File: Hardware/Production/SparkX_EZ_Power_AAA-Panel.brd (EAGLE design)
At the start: 187.2 x 136.7 mm, 1236 parts, among them J10 AVR_SPI_PROG_3X2TESTPOINTS, J12 AVR_SPI_PROG_3X2TESTPOINTS, J14 AVR_SPI_PROG_3X2TESTPOINTS, J16 AVR_SPI_PROG_3X2TESTPOINTS, J18 AVR_SPI_PROG_3X2TESTPOINTS, J20 AVR_SPI_PROG_3X2TESTPOINTS, J22 AVR_SPI_PROG_3X2TESTPOINTS, J24 AVR_SPI_PROG_3X2TESTPOINTS, J26 AVR_SPI_PROG_3X2TESTPOINTS, J28 AVR_SPI_PROG_3X2TESTPOINTS, J3 AVR_SPI_PROG_3X2TESTPOINTS, J30 AVR_SPI_PROG_3X2TESTPOINTS, J32 AVR_SPI_PROG_3X2TESTPOINTS, J34 AVR_SPI_PROG_3X2TESTPOINTS, J36 AVR_SPI_PROG_3X2TESTPOINTS, J38 AVR_SPI_PROG_3X2TESTPOINTS, J4 AVR_SPI_PROG_3X2TESTPOINTS, J40 AVR_SPI_PROG_3X2TESTPOINTS, J42 AVR_SPI_PROG_3X2TESTPOINTS, J44 AVR_SPI_PROG_3X2TESTPOINTS, J46 AVR_SPI_PROG_3X2TESTPOINTS, J48 AVR_SPI_PROG_3X2TESTPOINTS, J50 AVR_SPI_PROG_3X2TESTPOINTS, J52 AVR_SPI_PROG_3X2TESTPOINTS, J54 AVR_SPI_PROG_3X2TESTPOINTS, J56 AVR_SPI_PROG_3X2TESTPOINTS, J58 AVR_SPI_PROG_3X2TESTPOINTS, J6 AVR_SPI_PROG_3X2TESTPOINTS, J60 AVR_SPI_PROG_3X2TESTPOINTS, J8 AVR_SPI_PROG_3X2TESTPOINTS, U1 ATTINY43_QFN20, U10 TPS61200, U11 ATTINY43_QFN20, U12 TPS61200, U13 ATTINY43_QFN20, U14 TPS61200, U15 ATTINY43_QFN20, U16 TPS61200, U17 ATTINY43_QFN20, U18 TPS61200, U19 ATTINY43_QFN20, U2 TPS61200, U20 TPS61200, U21 ATTINY43_QFN20, U22 TPS61200, U23 ATTINY43_QFN20, U24 TPS61200, U25 ATTINY43_QFN20, U26 TPS61200, U27 ATTINY43_QFN20, U28 TPS61200, U29 ATTINY43_QFN20, U3 ATTINY43_QFN20, U30 TPS61200, U31 ATTINY43_QFN20, U32 TPS61200, U33 ATTINY43_QFN20, U34 TPS61200, U35 ATTINY43_QFN20, U36 TPS61200, U37 ATTINY43_QFN20, U38 TPS61200, U39 ATTINY43_QFN20, U4 TPS61200, U40 TPS61200, U41 ATTINY43_QFN20, U42 TPS61200, U43 ATTINY43_QFN20, U44 TPS61200, U45 ATTINY43_QFN20, U46 TPS61200, U47 ATTINY43_QFN20, U48 TPS61200, U49 ATTINY43_QFN20, U5 ATTINY43_QFN20, U50 TPS61200, U51 ATTINY43_QFN20, U52 TPS61200, U53 ATTINY43_QFN20, U54 TPS61200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

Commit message: Post-review updates
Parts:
- added RXD, RXD1, RXD10, RXD11, RXD12, RXD13, RXD14, RXD15, RXD16, RXD17, RXD18, RXD19, RXD2, RXD20, RXD21, RXD22, RXD23, RXD24, RXD25, RXD26, RXD27, RXD28, RXD29, RXD3, RXD4, RXD5, RXD6, RXD7, RXD8, RXD9, TXD, TXD1, TXD10, TXD11, TXD12, TXD13, TXD14, TXD15, TXD16, TXD17, TXD18, TXD19, TXD2, TXD20, TXD21, TXD22, TXD23, TXD24, TXD25, TXD26, TXD27, TXD28, TXD29, TXD3, TXD4, TXD5, TXD6, TXD7, TXD8, TXD9: TEST-POINT3X4, SparkFun-Connectors:PAD.03X.04
- added U$301, U$303, U$313, U$315, U$325, U$327, U$337, U$339, U$349, U$351: SPARKX-LOGO3, SparkX:SPARKX-SMALL
- added U$302, U$314, U$326, U$338, U$350: (no value), output:#OUT#0
- added U$304, U$316, U$328, U$340, U$352: (no value), output:#IN#0
- added U$305, U$317, U$329, U$341, U$353: (no value), output:#VIN#0
- added U$306, U$318, U$330, U$342, U$354: (no value), output:#3V3_EN#0
- added U$307, U$319, U$331, U$343, U$355: (no value), output:#PROC_PWR#0
- added U$308, U$320, U$332, U$344, U$356: (no value), output:#AT_VCC#0
- added U$309, U$310, U$321, U$322, U$333, U$334, U$345, U$346, U$357, U$358: (no value), output:EZ_POWER_AAA0
- added U$311, U$323, U$335, U$347, U$359: (no value), output:#TXD#0
- added U$312, U$324, U$336, U$348, U$360: (no value), output:#RXD#0
- C1, C103, C111, C119, C127, C135, C143, C15, C151, C159, C167, C175, C183, C191, C199, C207, C215, C223, C23, C231, C239, C31, C39, C47, C55, C63, C71, C79, C87, C95: device SparkFun-Capacitors:0603 -> SparkFun-Capacitors:0402-TIGHT
- C101, C102, C104, C109, C110, C112, C117, C118, C120, C125, C126, C128, C13, C133, C134, C136, C14, C141, C142, C144, C149, C150, C152, C157, C158, C16, C160, C165, C166, C168, C173, C174, C176, C181, C182, C184, C189, C190, C192, C197, C198, C2, C200, C205, C206, C208, C21, C213, C214, C216, C22, C221, C222, C224, C229, C230, C232, C237, C238, C24, C240, C29, C30, C32, C37, C38, C4, C40, C45, C46, C48, C53, C54, C56, C6, C61, C62, C64, C69, C70, C72, C77, C78, C80, C85, C86, C88, C93, C94, C96: device SparkFun-Capacitors:0402 -> SparkFun-Capacitors:0402-TIGHT
- L10, L12, L14, L16, L18, L2, L20, L22, L24, L26, L28, L30, L32, L34, L36, L38, L4, L40, L42, L44, L46, L48, L50, L52, L54, L56, L58, L6, L60, L8: value 4.7uH, 1.2A -> 4.7μH; device SparkFun:CDRH2D09 -> SparkFun-Coils:INDUCTOR_4X4MM
- R1, R10, R101, R102, R103, R105, R106, R107, R109, R11, R110, R111, R113, R114, R115, R117, R118, R119, R13, R14, R15, R17, R18, R19, R2, R21, R22, R23, R25, R26, R27, R29, R3, R30, R31, R33, R34, R35, R37, R38, R39, R41, R42, R43, R45, R46, R47, R49, R5, R50, R51, R53, R54, R55, R57, R58, R59, R6, R61, R62, R63, R65, R66, R67, R69, R7, R70, R71, R73, R74, R75, R77, R78, R79, R81, R82, R83, R85, R86, R87, R89, R9, R90, R91, R93, R94, R95, R97, R98, R99: device SparkFun-Resistors:0603 -> New-Parts_SparkFun-Resistors:0402-TIGHT
- U$100, U$160, U$220, U$280, U$40: device output:EZ_POWER_AAA0 -> output:#IN#0
- U$101, U$113, U$161, U$173, U$221, U$233, U$281, U$293, U$41, U$53: value SPARKX-LOGO3 -> (none); device SparkX:SPARKX-SMALL -> output:#VIN#0
- U$102, U$162, U$222, U$282, U$42: device output:#OUT#0 -> output:#3V3_EN#0
- U$103, U$151, U$163, U$211, U$223, U$271, U$283, U$31, U$43, U$91: value SPARKX-LOGO3 -> (none); device SparkX:SPARKX-SMALL -> output:#PROC_PWR#0
- U$104, U$164, U$224, U$284, U$44: device output:#IN#0 -> output:#AT_VCC#0
- U$105, U$165, U$225, U$285, U$45: device output:#VIN#0 -> output:EZ_POWER_AAA0
- U$106, U$166, U$226, U$286, U$46: device output:#3V3_EN#0 -> output:EZ_POWER_AAA0
- U$107, U$167, U$227, U$287, U$47: device output:#PROC_PWR#0 -> output:#TXD#0
- U$108, U$168, U$228, U$288, U$48: device output:#AT_VCC#0 -> output:#RXD#0
- U$109, U$159, U$169, U$219, U$229, U$279, U$289, U$39, U$49, U$99: value (none) -> SPARKX-LOGO3; device output:EZ_POWER_AAA0 -> SparkX:SPARKX-SMALL
- U$11, U$134, U$194, U$254, U$74: device output:#IN#0 -> output:#OUT#0
- U$110, U$170, U$230, U$290, U$50: device output:EZ_POWER_AAA0 -> output:#OUT#0
- U$112, U$172, U$232, U$292, U$52: device output:#OUT#0 -> output:#IN#0
- U$114, U$174, U$234, U$294, U$54: device output:#IN#0 -> output:#3V3_EN#0
- U$115, U$175, U$235, U$295, U$55: device output:#VIN#0 -> output:#PROC_PWR#0
- U$116, U$176, U$236, U$296, U$56: device output:#3V3_EN#0 -> output:#AT_VCC#0
- U$117, U$177, U$237, U$297, U$57: device output:#PROC_PWR#0 -> output:EZ_POWER_AAA0
- U$118, U$178, U$238, U$298, U$58: device output:#AT_VCC#0 -> output:EZ_POWER_AAA0
- U$119, U$179, U$239, U$299, U$59: device output:EZ_POWER_AAA0 -> output:#TXD#0
- U$120, U$180, U$240, U$300, U$60: device output:EZ_POWER_AAA0 -> output:#RXD#0
- U$131, U$143, U$191, U$203, U$23, U$251, U$263, U$4, U$71, U$83: value SPARKX-LOGO3 -> (none); device SparkX:SPARKX-SMALL -> output:#TXD#0
- U$132, U$192, U$252, U$72, U$9: device output:#OUT#0 -> output:#RXD#0
- U$135, U$14, U$145, U$195, U$205, U$25, U$255, U$265, U$75, U$85: value (none) -> SPARKX-LOGO3; device output:#VIN#0 -> SparkX:SPARKX-SMALL
- U$136, U$15, U$196, U$256, U$76: device output:#3V3_EN#0 -> output:#IN#0
- U$137, U$16, U$197, U$257, U$77: device output:#PROC_PWR#0 -> output:#VIN#0
- U$138, U$17, U$198, U$258, U$78: device output:#AT_VCC#0 -> output:#3V3_EN#0
- U$139, U$18, U$199, U$259, U$79: device output:EZ_POWER_AAA0 -> output:#PROC_PWR#0
- U$140, U$19, U$200, U$260, U$80: device output:EZ_POWER_AAA0 -> output:#AT_VCC#0
- U$141, U$153, U$201, U$21, U$213, U$261, U$273, U$33, U$81, U$93: value SPARKX-LOGO3 -> (none); device SparkX:SPARKX-SMALL -> output:EZ_POWER_AAA0
- U$142, U$202, U$22, U$262, U$82: device output:#OUT#0 -> output:EZ_POWER_AAA0
- U$144, U$204, U$24, U$264, U$84: device output:#IN#0 -> output:#RXD#0
- U$146, U$206, U$26, U$266, U$86: device output:#3V3_EN#0 -> output:#OUT#0
- U$147, U$157, U$207, U$217, U$267, U$27, U$277, U$37, U$87, U$97: value (none) -> SPARKX-LOGO3; device output:#PROC_PWR#0 -> SparkX:SPARKX-SMALL
- U$148, U$208, U$268, U$28, U$88: device output:#AT_VCC#0 -> output:#IN#0
- U$149, U$209, U$269, U$29, U$89: device output:EZ_POWER_AAA0 -> output:#VIN#0
- U$150, U$210, U$270, U$30, U$90: device output:EZ_POWER_AAA0 -> output:#3V3_EN#0
- U$152, U$212, U$272, U$32, U$92: device output:#OUT#0 -> output:#AT_VCC#0
- U$154, U$214, U$274, U$34, U$94: device output:#IN#0 -> output:EZ_POWER_AAA0
- U$155, U$215, U$275, U$35, U$95: device output:#VIN#0 -> output:#TXD#0
- U$156, U$216, U$276, U$36, U$96: device output:#3V3_EN#0 -> output:#RXD#0
- U$158, U$218, U$278, U$38, U$98: device output:#AT_VCC#0 -> output:#OUT#0
- U10, U12, U14, U16, U18, U2, U20, U22, U24, U26, U28, U30, U32, U34, U36, U38, U4, U40, U42, U44, U46, U48, U50, U52, U54, U56, U58, U6, U60, U8: device SparkFun:QFN-10_PAD -> SparkFun-IC-Power:QFN-10_PAD
- moved U$110 159.3 mm to (151.6, 4.89), flipped to the top
- moved U$105 150.5 mm to (139.7, 9.02), flipped to the top, turned to 90 degrees
- moved U$115 148.2 mm to (150.7, 3.75)
- moved U$103 145.3 mm to (134.5, 3.75)
- moved U$101 143.7 mm to (135.4, 10.2), flipped to the bottom
- moved U$113 143.4 mm to (151.7, 10.2)
- moved U$109 143.2 mm to (151.6, 30.0), turned to 0 degrees
- moved U$114 143.2 mm to (150.7, 14.0)
- moved U$104 141.5 mm to (135.4, 20.3), flipped to the top
- moved U$117 140.0 mm to (156.0, 9.02), flipped to the top, turned to 90 degrees
- moved U$111 137.0 mm to (151.6, 27.9), flipped to the bottom
- moved U$116 135.6 mm to (151.6, 20.3), flipped to the top
- moved U$118 134.8 mm to (151.6, 26.0), flipped to the bottom
- moved U$106 134.2 mm to (135.4, 26.0)
- moved U$120 134.0 mm to (150.3, 30.5)
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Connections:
- new net RXD: RXD.1, U1.16
- new net RXD1: RXD1.1, U3.16
- new net RXD10: RXD10.1, U21.16
- new net RXD11: RXD11.1, U23.16
- new net RXD12: RXD12.1, U25.16
- new net RXD13: RXD13.1, U27.16
- new net RXD14: RXD14.1, U29.16
- new net RXD15: RXD15.1, U31.16
- new net RXD16: RXD16.1, U33.16
- new net RXD17: RXD17.1, U35.16
- new net RXD18: RXD18.1, U37.16
- new net RXD19: RXD19.1, U39.16
- new net RXD2: RXD2.1, U5.16
- new net RXD20: RXD20.1, U41.16
- new net RXD21: RXD21.1, U43.16
- new net RXD22: RXD22.1, U45.16
- new net RXD23: RXD23.1, U47.16
- new net RXD24: RXD24.1, U49.16
- new net RXD25: RXD25.1, U51.16
- new net RXD26: RXD26.1, U53.16
- new net RXD27: RXD27.1, U55.16
- new net RXD28: RXD28.1, U57.16
- new net RXD29: RXD29.1, U59.16
- new net RXD3: RXD3.1, U7.16
- new net RXD4: RXD4.1, U9.16
- new net RXD5: RXD5.1, U11.16
- new net RXD6: RXD6.1, U13.16
- new net RXD7: RXD7.1, U15.16
- new net RXD8: RXD8.1, U17.16
- new net RXD9: RXD9.1, U19.16
- new net TXD: TXD.1, U1.15
- new net TXD1: TXD1.1, U3.15
- new net TXD10: TXD10.1, U21.15
- new net TXD11: TXD11.1, U23.15
- new net TXD12: TXD12.1, U25.15
- new net TXD13: TXD13.1, U27.15
- new net TXD14: TXD14.1, U29.15
- new net TXD15: TXD15.1, U31.15
- new net TXD16: TXD16.1, U33.15
- new net TXD17: TXD17.1, U35.15
- new net TXD18: TXD18.1, U37.15
- new net TXD19: TXD19.1, U39.15
- new net TXD2: TXD2.1, U5.15
- new net TXD20: TXD20.1, U41.15
- new net TXD21: TXD21.1, U43.15
- new net TXD22: TXD22.1, U45.15
- new net TXD23: TXD23.1, U47.15
- new net TXD24: TXD24.1, U49.15
- new net TXD25: TXD25.1, U51.15
- new net TXD26: TXD26.1, U53.15
- new net TXD27: TXD27.1, U55.15
- new net TXD28: TXD28.1, U57.15
- new net TXD29: TXD29.1, U59.15
- new net TXD3: TXD3.1, U7.15
- new net TXD4: TXD4.1, U9.15
- new net TXD5: TXD5.1, U11.15
- new net TXD6: TXD6.1, U13.15
- new net TXD7: TXD7.1, U15.15
- new net TXD8: TXD8.1, U17.15
- new net TXD9: TXD9.1, U19.15
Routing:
- net VIN29: track 57.7 -> 46.2 mm
- net VIN18: track 57.7 -> 46.2 mm
- net VIN9: track 57.7 -> 46.2 mm
- net VIN8: track 57.7 -> 46.2 mm
- net VIN28: track 57.7 -> 46.2 mm
- net VIN19: track 57.7 -> 46.2 mm
- net VIN23: track 57.7 -> 46.2 mm
- net VIN: track 57.7 -> 46.2 mm
- net VIN22: track 57.7 -> 46.2 mm
- net VIN3: track 57.7 -> 46.2 mm
- net VIN13: track 57.7 -> 46.2 mm
- net VIN1: track 57.7 -> 46.2 mm
- net VIN21: track 57.7 -> 46.2 mm
- net VIN20: track 57.7 -> 46.2 mm
- net VIN11: track 57.7 -> 46.2 mm
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
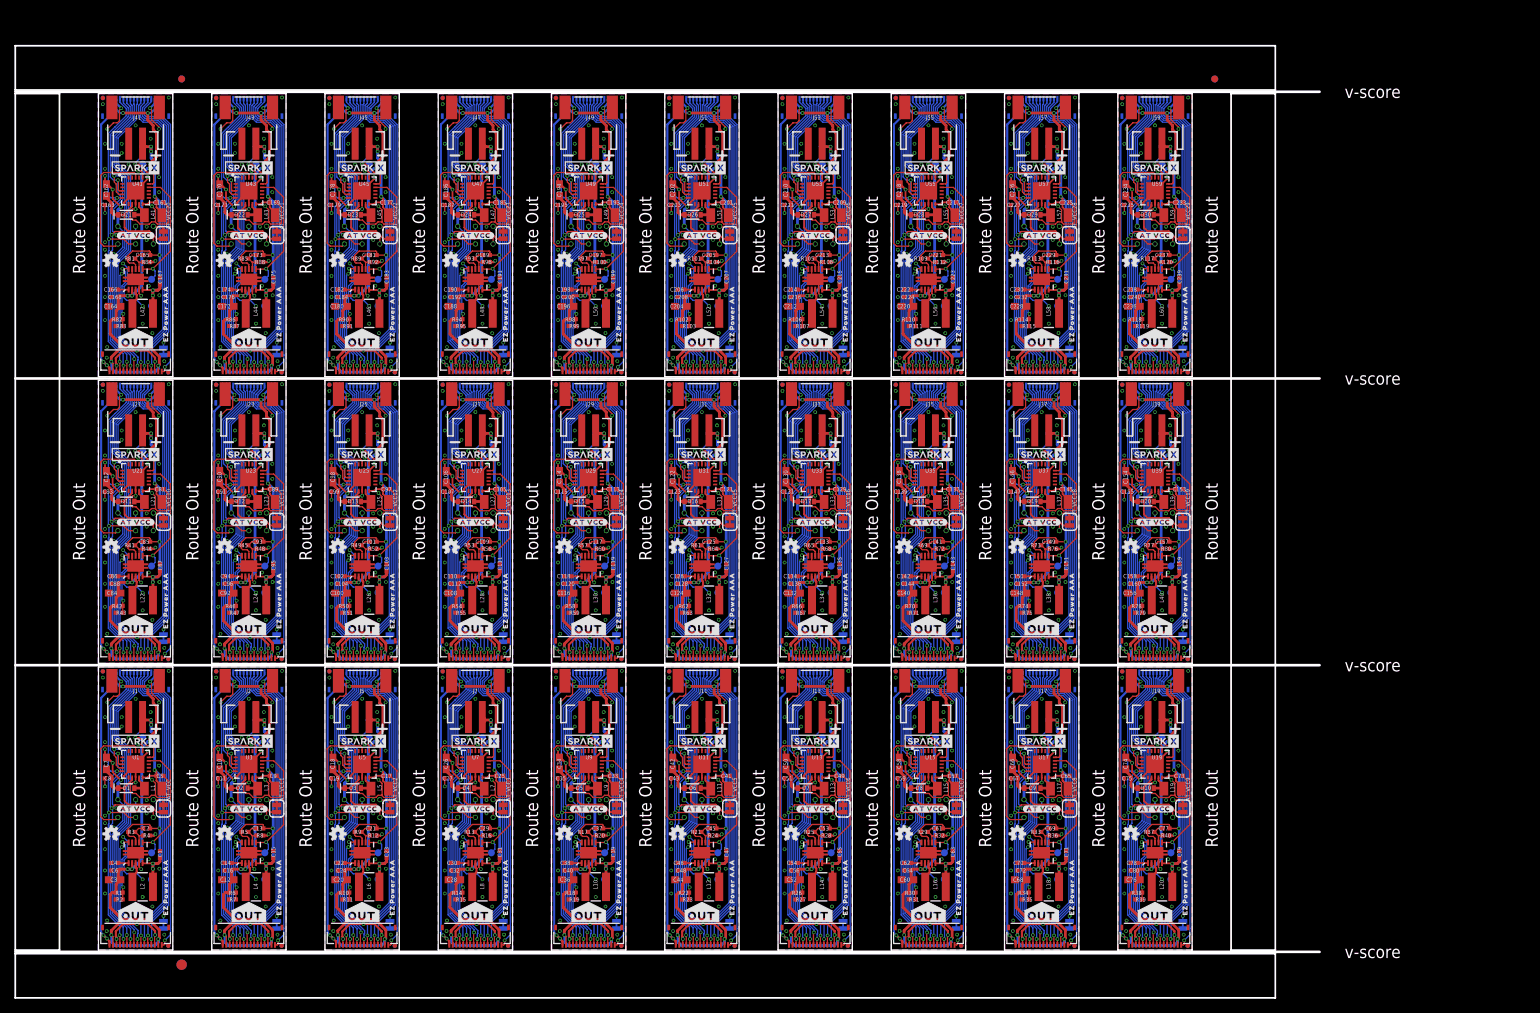
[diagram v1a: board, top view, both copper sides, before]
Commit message: Add VIN Max 5.5V
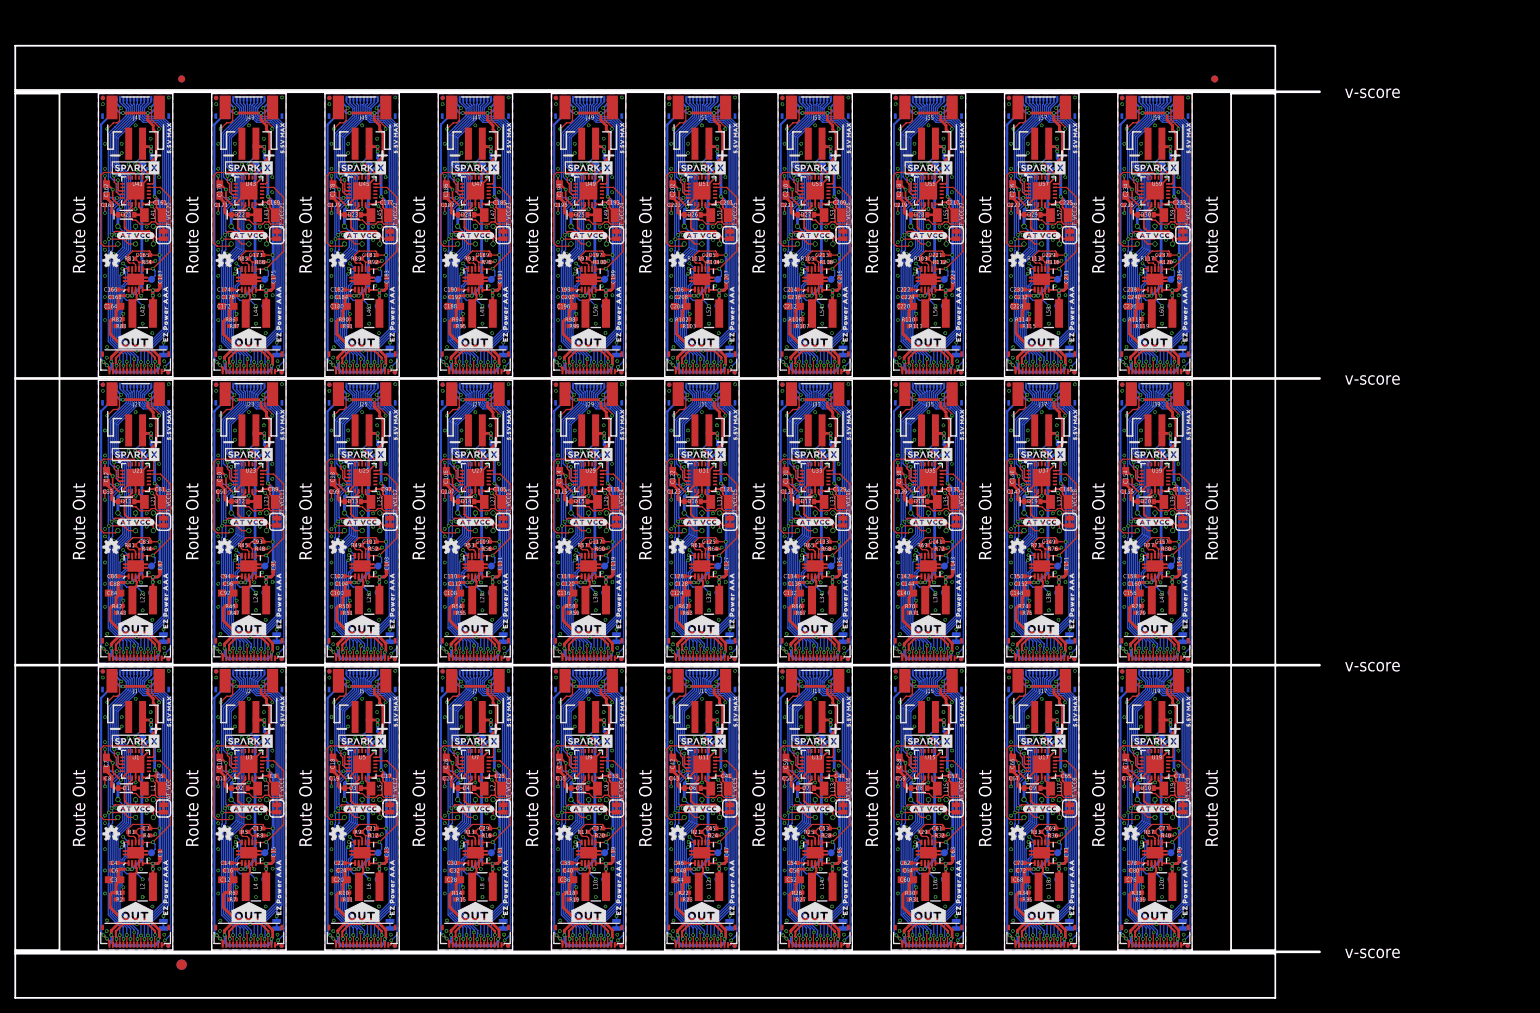
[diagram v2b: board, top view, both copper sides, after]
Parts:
- added U$361, U$373, U$374, U$386, U$387: (no value), output:EZ_POWER_AAA0
- added U$362, U$375, U$388: (no value), output:#TXD#0
- added U$363, U$376, U$389: (no value), output:#RXD#0
- added U$364, U$377, U$390: (no value), output:5#5V_MAX0
- added U$365, U$367, U$378, U$380: SPARKX-LOGO3, SparkX:SPARKX-SMALL
- added U$366, U$379: (no value), output:#OUT#0
- added U$368, U$381: (no value), output:#IN#0
- added U$369, U$382: (no value), output:#VIN#0
- added U$370, U$383: (no value), output:#3V3_EN#0
- added U$371, U$384: (no value), output:#PROC_PWR#0
- added U$372, U$385: (no value), output:#AT_VCC#0
- U$10, U$169, U$195, U$325, U$351, U$39: value SPARKX-LOGO3 -> (none); device SparkX:SPARKX-SMALL -> output:5#5V_MAX0
- U$100, U$244, U$256, U$88: device output:#IN#0 -> output:EZ_POWER_AAA0
- U$101, U$113, U$257, U$269: device output:#VIN#0 -> output:EZ_POWER_AAA0
- U$102, U$258: device output:#3V3_EN#0 -> output:#TXD#0
- U$103, U$259: device output:#PROC_PWR#0 -> output:#RXD#0
- U$104, U$260: device output:#AT_VCC#0 -> output:5#5V_MAX0
- U$105, U$118, U$237, U$250, U$261, U$274, U$81, U$94: value (none) -> SPARKX-LOGO3; device output:EZ_POWER_AAA0 -> SparkX:SPARKX-SMALL
- U$106, U$249, U$262, U$93: device output:EZ_POWER_AAA0 -> output:#OUT#0
- U$107, U$131, U$263, U$287: value (none) -> SPARKX-LOGO3; device output:#TXD#0 -> SparkX:SPARKX-SMALL
- U$108, U$264: device output:#RXD#0 -> output:#IN#0
- U$109, U$135, U$265, U$291: value SPARKX-LOGO3 -> (none); device SparkX:SPARKX-SMALL -> output:#VIN#0
- U$11, U$146, U$170, U$302, U$326: value (none) -> SPARKX-LOGO3; device output:#OUT#0 -> SparkX:SPARKX-SMALL
- U$110, U$266: device output:#OUT#0 -> output:#3V3_EN#0
- U$111, U$241, U$267, U$85: value SPARKX-LOGO3 -> (none); device SparkX:SPARKX-SMALL -> output:#PROC_PWR#0
- U$112, U$268: device output:#IN#0 -> output:#AT_VCC#0
- U$114, U$126, U$270, U$282: device output:#3V3_EN#0 -> output:EZ_POWER_AAA0
- U$115, U$271: device output:#PROC_PWR#0 -> output:#TXD#0
- U$116, U$272: device output:#AT_VCC#0 -> output:#RXD#0
- U$117, U$130, U$273, U$286: device output:EZ_POWER_AAA0 -> output:5#5V_MAX0
- U$119, U$275: device output:#TXD#0 -> output:#OUT#0
- U$120, U$144, U$276, U$300: value (none) -> SPARKX-LOGO3; device output:#RXD#0 -> SparkX:SPARKX-SMALL
- U$121, U$147, U$277, U$303: value SPARKX-LOGO3 -> (none); device SparkX:SPARKX-SMALL -> output:#IN#0
- U$122, U$278: device output:#OUT#0 -> output:#VIN#0
- U$123, U$253, U$279, U$97: value SPARKX-LOGO3 -> (none); device SparkX:SPARKX-SMALL -> output:#3V3_EN#0
- U$124, U$280: device output:#IN#0 -> output:#PROC_PWR#0
- U$125, U$281: device output:#VIN#0 -> output:#AT_VCC#0
- U$127, U$139, U$283, U$295: device output:#PROC_PWR#0 -> output:EZ_POWER_AAA0
- U$128, U$284: device output:#AT_VCC#0 -> output:#TXD#0
- U$129, U$142, U$285, U$298: device output:EZ_POWER_AAA0 -> output:#RXD#0
- U$132, U$288: device output:#RXD#0 -> output:#OUT#0
- U$134, U$290: device output:#OUT#0 -> output:#IN#0
- U$136, U$292: device output:#IN#0 -> output:#3V3_EN#0
- U$137, U$293: device output:#VIN#0 -> output:#PROC_PWR#0
- U$138, U$294: device output:#3V3_EN#0 -> output:#AT_VCC#0
- U$14, U$145, U$171, U$301, U$327: value SPARKX-LOGO3 -> (none); device SparkX:SPARKX-SMALL -> output:#OUT#0
- U$140, U$152, U$296, U$308: device output:#AT_VCC#0 -> output:EZ_POWER_AAA0
- U$141, U$154, U$297, U$310: device output:EZ_POWER_AAA0 -> output:#TXD#0
- U$143, U$299: device output:#TXD#0 -> output:5#5V_MAX0
- U$148, U$304: device output:#IN#0 -> output:#VIN#0
- U$149, U$305: device output:#VIN#0 -> output:#3V3_EN#0
- U$15, U$172, U$196, U$328, U$352, U$40: value (none) -> SPARKX-LOGO3; device output:#IN#0 -> SparkX:SPARKX-SMALL
- U$150, U$306: device output:#3V3_EN#0 -> output:#PROC_PWR#0
- U$151, U$307: device output:#PROC_PWR#0 -> output:#AT_VCC#0
- U$155, U$311: device output:#TXD#0 -> output:#RXD#0
- U$156, U$312: device output:#RXD#0 -> output:5#5V_MAX0
- U$16, U$173, U$329: device output:#VIN#0 -> output:#IN#0
- U$17, U$174, U$330: device output:#3V3_EN#0 -> output:#VIN#0
- U$175, U$18, U$331: device output:#PROC_PWR#0 -> output:#3V3_EN#0
- U$176, U$19, U$332: device output:#AT_VCC#0 -> output:#PROC_PWR#0
- U$177, U$190, U$21, U$333, U$34, U$346: device output:EZ_POWER_AAA0 -> output:#AT_VCC#0
- U$179, U$191, U$23, U$335, U$347, U$35: device output:#TXD#0 -> output:EZ_POWER_AAA0
- U$180, U$24, U$336: device output:#RXD#0 -> output:#TXD#0
- U$181, U$207, U$25, U$337, U$51: value SPARKX-LOGO3 -> (none); device SparkX:SPARKX-SMALL -> output:#RXD#0
- U$182, U$26, U$338: device output:#OUT#0 -> output:5#5V_MAX0
- U$184, U$28, U$340: device output:#IN#0 -> output:#OUT#0
- U$185, U$209, U$29, U$341, U$53: value (none) -> SPARKX-LOGO3; device output:#VIN#0 -> SparkX:SPARKX-SMALL
- U$186, U$30, U$342: device output:#3V3_EN#0 -> output:#IN#0
- U$187, U$31, U$343: device output:#PROC_PWR#0 -> output:#VIN#0
- U$188, U$32, U$344: device output:#AT_VCC#0 -> output:#3V3_EN#0
- U$189, U$202, U$33, U$345, U$358, U$46: device output:EZ_POWER_AAA0 -> output:#PROC_PWR#0
- U$192, U$204, U$348, U$36, U$360, U$48: device output:#RXD#0 -> output:EZ_POWER_AAA0
- U$193, U$219, U$349, U$37, U$63: value SPARKX-LOGO3 -> (none); device SparkX:SPARKX-SMALL -> output:#TXD#0
- U$194, U$350, U$38: device output:#OUT#0 -> output:#RXD#0
- U$197, U$353, U$41: device output:#VIN#0 -> output:#OUT#0
- U$198, U$222, U$354, U$42, U$66: value (none) -> SPARKX-LOGO3; device output:#3V3_EN#0 -> SparkX:SPARKX-SMALL
- U$199, U$355, U$43: device output:#PROC_PWR#0 -> output:#IN#0
- U$200, U$356, U$44: device output:#AT_VCC#0 -> output:#VIN#0
- U$201, U$214, U$357, U$45, U$58: device output:EZ_POWER_AAA0 -> output:#3V3_EN#0
- U$203, U$359, U$47: device output:#TXD#0 -> output:#AT_VCC#0
- U$205, U$217, U$231, U$243, U$49, U$61, U$75, U$87: value SPARKX-LOGO3 -> (none); device SparkX:SPARKX-SMALL -> output:EZ_POWER_AAA0
- U$206, U$50: device output:#OUT#0 -> output:#TXD#0
- U$208, U$52: device output:#IN#0 -> output:5#5V_MAX0
- U$210, U$54: device output:#3V3_EN#0 -> output:#OUT#0
- U$211, U$235, U$55, U$79: value (none) -> SPARKX-LOGO3; device output:#PROC_PWR#0 -> SparkX:SPARKX-SMALL
- U$212, U$56: device output:#AT_VCC#0 -> output:#IN#0
- U$213, U$226, U$57, U$70: device output:EZ_POWER_AAA0 -> output:#VIN#0
- U$215, U$59: device output:#TXD#0 -> output:#PROC_PWR#0
- U$216, U$60: device output:#RXD#0 -> output:#AT_VCC#0
- U$218, U$230, U$62, U$74: device output:#OUT#0 -> output:EZ_POWER_AAA0
- U$220, U$64: device output:#IN#0 -> output:#RXD#0
- U$221, U$65: device output:#VIN#0 -> output:5#5V_MAX0
- U$223, U$67: device output:#PROC_PWR#0 -> output:#OUT#0
- U$224, U$248, U$68, U$92: value (none) -> SPARKX-LOGO3; device output:#AT_VCC#0 -> SparkX:SPARKX-SMALL
- U$225, U$238, U$69, U$82: device output:EZ_POWER_AAA0 -> output:#IN#0
- U$227, U$71: device output:#TXD#0 -> output:#3V3_EN#0
- U$228, U$72: device output:#RXD#0 -> output:#PROC_PWR#0
- U$229, U$255, U$73, U$99: value SPARKX-LOGO3 -> (none); device SparkX:SPARKX-SMALL -> output:#AT_VCC#0
- U$232, U$76: device output:#IN#0 -> output:#TXD#0
- U$233, U$77: device output:#VIN#0 -> output:#RXD#0
- U$234, U$78: device output:#3V3_EN#0 -> output:5#5V_MAX0
- U$236, U$80: device output:#AT_VCC#0 -> output:#OUT#0
- U$239, U$83: device output:#TXD#0 -> output:#VIN#0
- U$240, U$84: device output:#RXD#0 -> output:#3V3_EN#0
- U$242, U$86: device output:#OUT#0 -> output:#AT_VCC#0
- U$245, U$89: device output:#VIN#0 -> output:#TXD#0
- U$246, U$90: device output:#3V3_EN#0 -> output:#RXD#0
- U$247, U$91: device output:#PROC_PWR#0 -> output:5#5V_MAX0
- U$251, U$95: device output:#TXD#0 -> output:#IN#0
- U$252, U$96: device output:#RXD#0 -> output:#VIN#0
- U$254, U$98: device output:#OUT#0 -> output:#PROC_PWR#0
- U1, U11, U13, U15, U17, U19, U21, U23, U25, U27, U29, U3, U31, U33, U35, U37, U39, U41, U43, U45, U47, U49, U5, U51, U53, U55, U57, U59, U7, U9: device New-Parts_SparkFun-IC-Microcontroller:QFN20_20M1 -> SparkFun-IC-Microcontroller:QFN20_20M1
- moved U$124 162.3 mm to (150.7, 3.75)
- moved U$252 160.0 mm to (151.7, 51.3)
- moved U$126 158.5 mm to (156.0, 9.02), flipped to the top, turned to 90 degrees
- moved U$123 155.4 mm to (150.7, 14.0)
- moved U$130 154.7 mm to (156.5, 34.3), flipped to the top, turned to 90 degrees
- moved U$251 152.9 mm to (151.6, 75.9)
- moved U$250 151.5 mm to (151.6, 69.1)
- moved U$121 150.7 mm to (151.6, 34.8), flipped to the bottom
- moved U$122 150.7 mm to (151.7, 10.2), flipped to the bottom
- moved U$256 150.1 mm to (156.0, 50.2), flipped to the top, turned to 90 degrees
- moved U$248 149.6 mm to (151.6, 71.1)
- moved U$125 149.5 mm to (151.6, 20.3), flipped to the top
- moved U$249 149.0 mm to (151.6, 46.0), turned to 0 degrees
- moved U$127 148.4 mm to (151.6, 26.0)
- moved U$128 147.7 mm to (150.2, 33.0), flipped to the bottom
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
